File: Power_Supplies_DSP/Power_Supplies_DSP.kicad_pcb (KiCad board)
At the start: 4 copper layers, 130.8 x 58.8 mm, 46 parts, among them J1 PINHD_1x10_Male, J2 SBH11-PBPC-D10-ST-BK, J4 PINHD_1x10_Male, J5 PINHD_1x2_Female, J6 PINHD_1x10_Female, U2 STM32H755ZIT6, X3 NX3215SA-32.768K, X4 NX2016SA-32MHZ

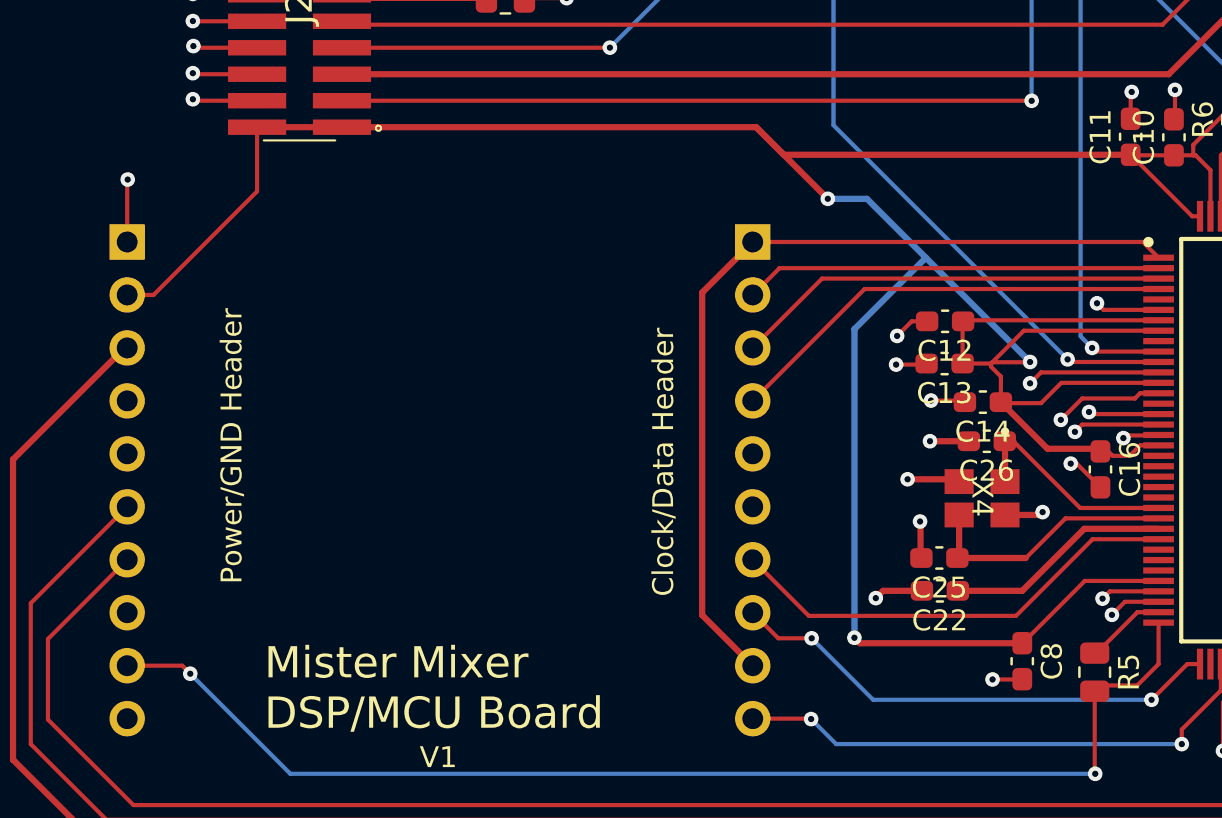
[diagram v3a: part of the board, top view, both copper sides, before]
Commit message: fixed an oopsie w/ 3.3V on mcu board
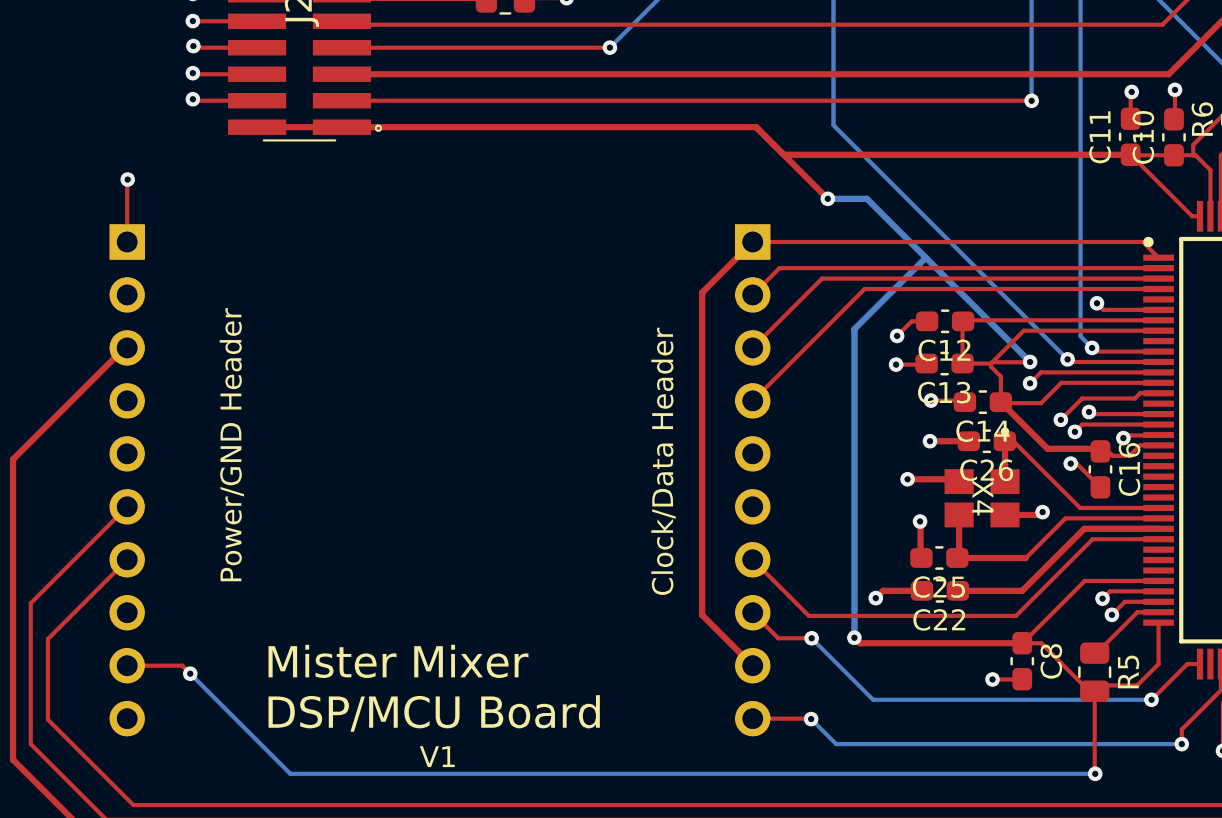
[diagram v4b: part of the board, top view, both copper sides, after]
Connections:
- J1 pad 2: 3.3V -> unconnected-(J1-Pad2)
- J1 pad 9: 3.3V_2 -> 3.3V
- R5 pad 2: 3.3V_2 -> 3.3V
- U2 pad 36: 3.3V_2 -> 3.3V
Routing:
- net 3.3V_2: track 58.0 -> 0.00 mm, vias 2 -> 0
- net 3.3V: track 331.8 -> 382.8 mm, vias 10 -> 12
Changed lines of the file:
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@@
 	(net 8 "3.3V")
 	(net 9 "unconnected-(J1-Pad5)")
-	(net 10 "3.3V_2")
+	(net 10 "unconnected-(J1-Pad2)")
 	(net 11 "unconnected-(J1-Pad4)")
 	(net 12 "unconnected-(J1-Pad8)")
@@
 			(layers "F.Cu" "F.Paste" "F.Mask")
 			(roundrect_rratio 0.243902)
-			(net 10 "3.3V_2")
+			(net 8 "3.3V")
 			(pintype "passive")
 		)
@@
 			(size 0.3 1.475)
 			(layers "F.Cu" "F.Paste" "F.Mask")
-			(net 10 "3.3V_2")
+			(net 8 "3.3V")
 			(pinfunction "VDDA")
 			(pintype "power_in")
@@
 			(layers "*.Cu" "*.Mask")
 			(remove_unused_layers no)
-			(net 8 "3.3V")
+			(net 10 "unconnected-(J1-Pad2)")
 			(pintype "passive")
 		)
@@
 			(layers "*.Cu" "*.Mask")
 			(remove_unused_layers no)
-			(net 10 "3.3V_2")
+			(net 8 "3.3V")
 			(pintype "passive")
 		)
@@
 	)
 	(segment
+		(start 199.6125 163.0375)
+		(end 197.6 163.0375)
+		(width 0.2)
+		(layer "F.Cu")
+		(net 8)
+	)
+	(segment
 		(start 222.1505 156.9875)
 		(end 222.113 157.025)
@@
 	)
 	(segment
+		(start 197.3125 163.3125)
+		(end 197.575 163.3125)
+		(width 0.2)
+		(layer "F.Cu")
+		(net 8)
+	)
+	(segment
 		(start 218.85 165.6375)
 		(end 219.125 165.3625)
@@
 	)
 	(segment
-		(start 151.175 144.31)
-		(end 152.44 144.31)
-		(width 0.2)
-		(layer "F.Cu")
-		(net 8)
-	)
-	(segment
 		(start 225.65 156.9875)
 		(end 222.1505 156.9875)
@@
 	)
 	(segment
-		(start 192.6 147.6)
-		(end 192.6625 147.5375)
+		(start 197.575 167.25)
+		(end 197.6 167.275)
 		(width 0.2)
 		(layer "F.Cu")
@@
 	)
 	(segment
-		(start 204.425 134.875)
-		(end 205.85 133.45)
+		(start 192.6 147.6)
+		(end 192.6625 147.5375)
 		(width 0.2)
 		(layer "F.Cu")
@@
 	)
 	(segment
-		(start 152.44 144.31)
-		(end 157.405 139.345)
+		(start 204.425 134.875)
+		(end 205.85 133.45)
 		(width 0.2)
 		(layer "F.Cu")
@@
 	)
 	(segment
+		(start 153.815 162.09)
+		(end 154.2 162.475)
+		(width 0.2)
+		(layer "F.Cu")
+		(net 8)
+	)
+	(segment
 		(start 205.2375 164.2)
 		(end 205.2375 165.2375)
@@
 	)
 	(segment
+		(start 200.637 160.025)
+		(end 200.637 162.013)
+		(width 0.2)
+		(layer "F.Cu")
+		(net 8)
+	)
+	(segment
 		(start 200.637 146.025)
 		(end 194.175 146.025)
@@
 	)
 	(segment
-		(start 157.405 139.345)
-		(end 157.405 136.265)
+		(start 197.575 163.3125)
+		(end 197.575 167.25)
 		(width 0.2)
 		(layer "F.Cu")
@@
 	)
 	(segment
+		(start 151.175 162.09)
+		(end 153.815 162.09)
+		(width 0.2)
+		(layer "F.Cu")
+		(net 8)
+	)
+	(segment
 		(start 225.65 156.9875)
 		(end 225.65 158.9)
@@
 	)
 	(segment
+		(start 200.637 162.013)
+		(end 199.6125 163.0375)
+		(width 0.2)
+		(layer "F.Cu")
+		(net 8)
+	)
+	(segment
 		(start 205.125 162.013)
 		(end 205.125 164.0875)
@@
 	)
 	(segment
+		(start 195.0125 161.0125)
+		(end 197.3125 163.3125)
+		(width 0.2)
+		(layer "F.Cu")
+		(net 8)
+	)
+	(segment
 		(start 217.825 137.825)
 		(end 221.575 134.075)
@@
 		(net 8)
 	)
+	(segment
+		(start 195.0125 161.0125)
+		(end 194.1 161.0125)
+		(width 0.2)
+		(layer "F.Cu")
+		(net 8)
+	)
+	(via
+		(at 154.2 162.475)
+		(size 0.7)
+		(drill 0.3)
+		(layers "F.Cu" "B.Cu")
+		(net 8)
+	)
 	(via
 		(at 194.475 147.525)
@@
 	)
 	(via
+		(at 197.6 167.275)
+		(size 0.7)
+		(drill 0.3)
+		(layers "F.Cu" "B.Cu")
+		(net 8)
+	)
+	(via
 		(at 224.475 149.45)
 		(size 0.7)
@@
 	)
 	(segment
+		(start 197.6 167.275)
+		(end 159 167.275)
+		(width 0.2)
+		(layer "B.Cu")
+		(net 8)
+	)
+	(segment
+		(start 159 167.275)
+		(end 154.2 162.475)
+		(width 0.2)
+		(layer "B.Cu")
+		(net 8)
+	)
+	(segment
 		(start 227.1 158.9)
 		(end 227.075 158.925)
@@
 	)
 	(segment
-		(start 199.6125 163.0375)
-		(end 197.6 163.0375)
-		(width 0.2)
-		(layer "F.Cu")
-		(net 10)
-	)
-	(segment
-		(start 197.575 167.25)
-		(end 197.6 167.275)
-		(width 0.2)
-		(layer "F.Cu")
-		(net 10)
-	)
-	(segment
-		(start 153.815 162.09)
-		(end 154.2 162.475)
-		(width 0.2)
-		(layer "F.Cu")
-		(net 10)
-	)
-	(segment
-		(start 200.637 160.025)
-		(end 200.637 162.013)
-		(width 0.2)
-		(layer "F.Cu")
-		(net 10)
-	)
-	(segment
-		(start 197.575 163.3125)
-		(end 197.575 167.25)
-		(width 0.2)
-		(layer "F.Cu")
-		(net 10)
-	)
-	(segment
-		(start 151.175 162.09)
-		(end 153.815 162.09)
-		(width 0.2)
-		(layer "F.Cu")
-		(net 10)
-	)
-	(segment
-		(start 200.637 162.013)
-		(end 199.6125 163.0375)
-		(width 0.2)
-		(layer "F.Cu")
-		(net 10)
-	)
-	(via
-		(at 154.2 162.475)
-		(size 0.7)
-		(drill 0.3)
-		(layers "F.Cu" "B.Cu")
-		(net 10)
-	)
-	(via
-		(at 197.6 167.275)
-		(size 0.7)
-		(drill 0.3)
-		(layers "F.Cu" "B.Cu")
-		(net 10)
-	)
-	(segment
-		(start 197.6 167.275)
-		(end 159 167.275)
-		(width 0.2)
-		(layer "B.Cu")
-		(net 10)
-	)
-	(segment
-		(start 159 167.275)
-		(end 154.2 162.475)
-		(width 0.2)
-		(layer "B.Cu")
-		(net 10)
-	)
-	(segment

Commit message: stuff i may or may not have done to order these things
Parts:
- removed J2: SBH11-PBPC-D10-ST-BK, SamacSys_Parts:FTSH-110-XX-YYY-DV-K
- added J7: SBH11-PBPC-D10-ST-BK, SamacSys_Parts:SHDR20W64P254_2X10_2794X910X880P, F.Cu at (147.9, 123.0)
- X3: footprint Inductor_SMD:L_6.3x6.3_H3 -> SamacSys_Parts:NX3215SA32768KSTDMUA8
- X4: footprint SamacSys_Parts:FA-238_EPS -> SamacSys_Parts:NX2016SA32MHZEXS00ACS06654
- moved R15 11.1 mm to (178.9, 122.8), turned to 180 degrees
- moved R14 11.0 mm to (178.9, 125.1), turned to 180 degrees
- moved R13 6.22 mm to (163.2, 128.7), turned to 90 degrees
- turned X4 to 180 degrees
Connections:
- R13 pad 1: Net-(J2-Pad11) -> GND
- R13 pad 2: GND -> Net-(J7-Pad11)
- R14 pad 1: Net-(J2-Pad17) -> GND
- R14 pad 2: GND -> Net-(J7-Pad17)
- R15 pad 1: Net-(J2-Pad19) -> GND
- R15 pad 2: GND -> Net-(J7-Pad19)
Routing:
- net 3.3V: track 382.8 -> 399.6 mm
- net JTRST: track 67.2 -> 83.8 mm
- net JTDI: track 83.2 -> 97.4 mm
- net SWDIO: track 102.3 -> 114.3 mm
- net Net-(J7-Pad17): track 0.00 -> 10.6 mm
- net SWCLK: track 88.6 -> 98.3 mm
- net Net-(J7-Pad19): track 0.00 -> 7.71 mm
- net Net-(J2-Pad19): track 7.64 -> 0.00 mm
- net Net-(J2-Pad11): track 7.08 -> 0.00 mm
- net Net-(J2-Pad17): track 6.83 -> 0.00 mm
- net Net-(J7-Pad11): track 0.00 -> 5.91 mm
- net Net-(U2A-PC15-OSC32_OUT): track 37.5 -> 39.0 mm
- net Net-(U2A-PC14-OSC32_IN): track 31.8 -> 33.3 mm
- net GND: track 156.0 -> 154.6 mm, vias 62 -> 59
- net Net-(U2B-PH1-OSC_OUT): track 12.1 -> 13.0 mm
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- added copper zone on F.Cu, net GND
